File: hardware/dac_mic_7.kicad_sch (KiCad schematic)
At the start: 29 parts, among them J6 IMP34DT05, J7 SJ-3524-SMT, U6 CS43L22

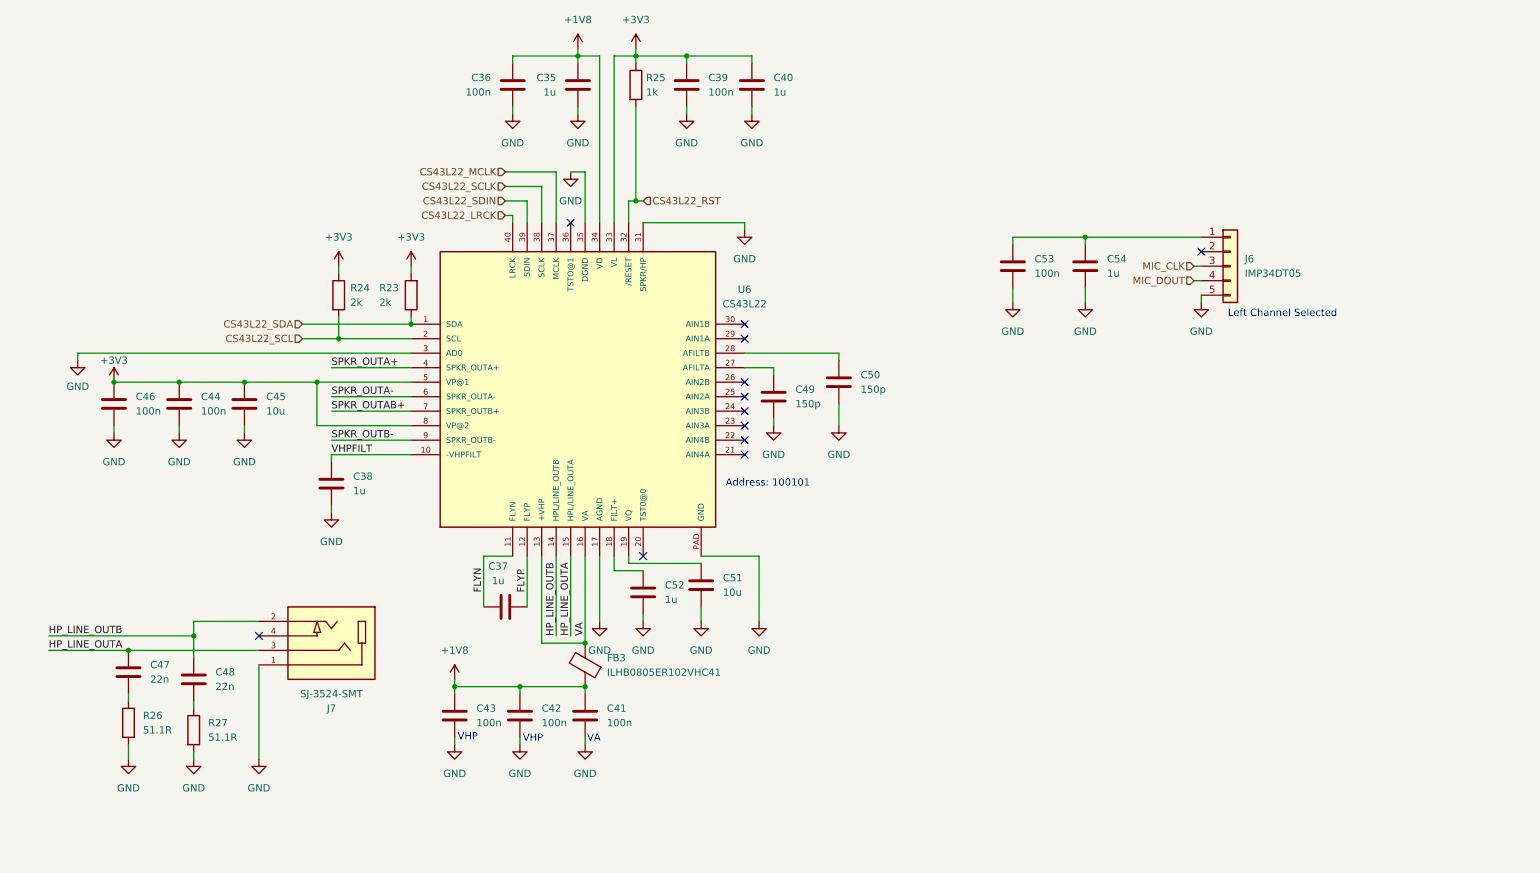
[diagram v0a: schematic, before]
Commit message: Design Schematic for STM32F407
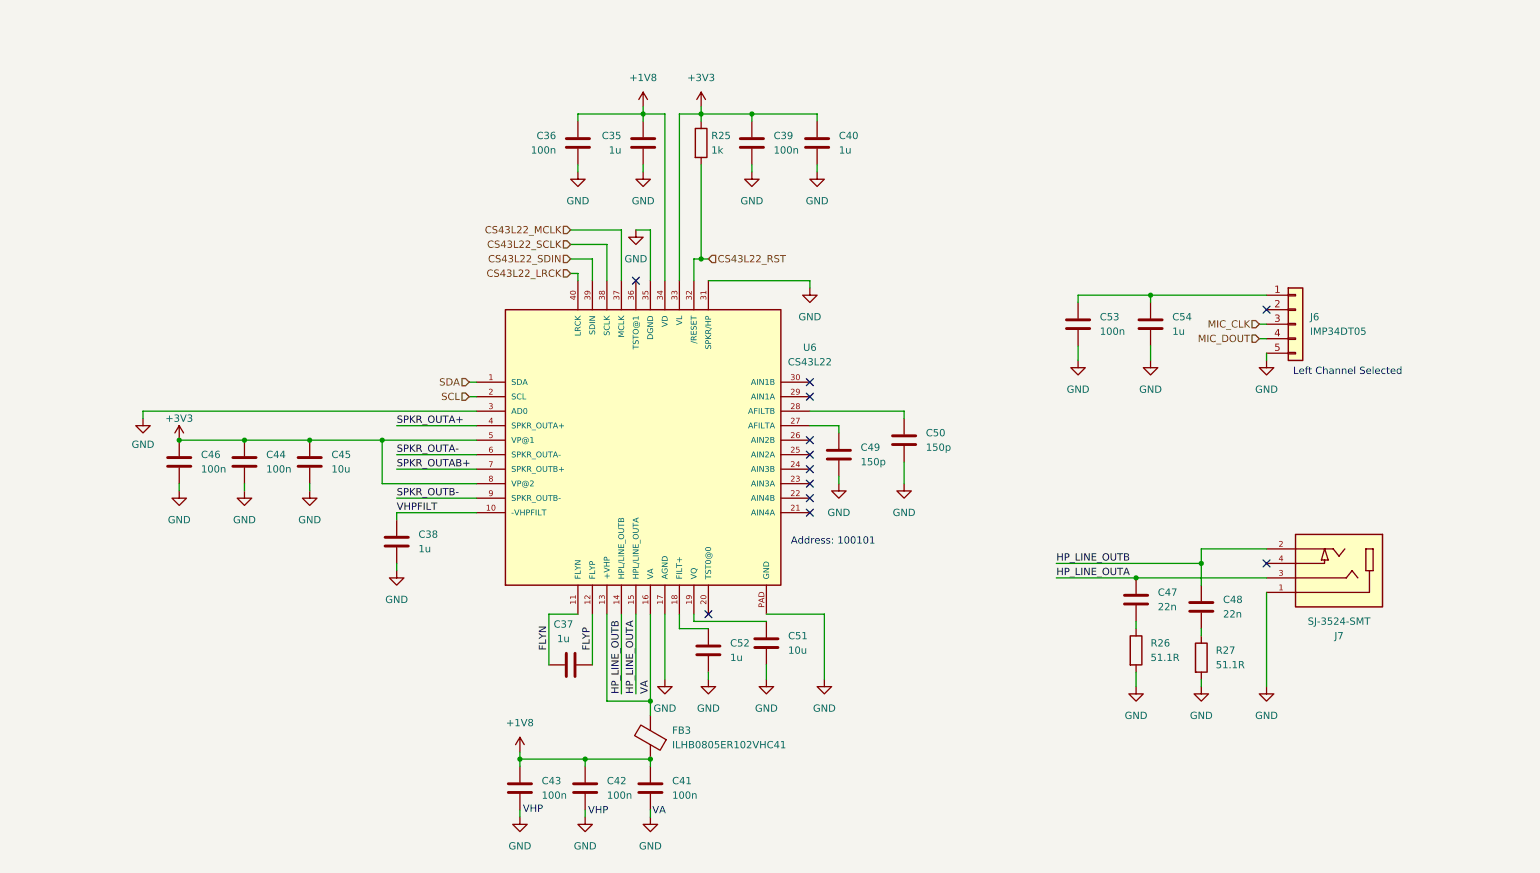
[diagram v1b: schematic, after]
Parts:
- removed R23, R24: 2k, symbol Device:R
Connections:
- net CS43L22_SCL renamed SCL
- net CS43L22_SDA renamed SDA
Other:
- moved on the sheet: C35, C36, C37, C38, C39, C40, C41, C42, C43, C44, C45, C46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

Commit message: Complete Schematic for Power Section
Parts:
- renumbered C46 to C34, C44 to C35, C45 to C36, C38 to C37, C43 to C38, C37 to C39, C36 to C40, C42 to C41, C35 to C42, C41 to C43, C52 to C44, C39 to C45, C51 to C46, C40 to C47, C49 to C48, C50 to C49, C53 to C50, C47 to C51, C54 to C52, C48 to C53, R25 to R20, R26 to R21, R27 to R22

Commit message: Organize schematic
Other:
- note added: "DAC"
- note added: "Headphones"
- note added: "Mic"
- moved on the sheet: C34, C35, C36, C37, C38, C39, C40, C41, C42, C43, C44, C45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

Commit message: Link footprints to Symbols
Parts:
- C34, C35, C40, C45, C49, C50: footprint (none) -> STM32F407 Dev Kit Library:C_0805_2012Metric_Pad1.18x1.45mm_HandSolder
- C36, C42, C47, C52: footprint SODFL1006X43N -> STM32F407 Dev Kit Library:C_0805_2012Metric_Pad1.18x1.45mm_HandSolder
- C37, C38, C39, C41, C43, C44, C46, C48, C51, C53: footprint Diode_SMD:ST_D_SMC -> STM32F407 Dev Kit Library:C_0805_2012Metric_Pad1.18x1.45mm_HandSolder
- FB3: footprint Package_DFN_QFN:QFN-16-1EP_4x4mm_P0.65mm_EP2.1x2.1mm -> STM32F407 Dev Kit Library:C_0805_2012Metric_Pad1.18x1.45mm_HandSolder
- J6: footprint Package_DFN_QFN:QFN-20-1EP_5x5mm_P0.65mm_EP3.35x3.35mm -> STM32F407 Dev Kit Library:IMP34DT06JTR
- J7: footprint SJ-3524-SMT:CUI_SJ-3524-SMT -> STM32F407 Dev Kit Library:SJ-3524-SMT
- R20, R21, R22: footprint (none) -> STM32F407 Dev Kit Library:R_0805_2012Metric_Pad1.20x1.40mm_HandSolder
- U6: footprint CS43L22:QFN40-6X6 -> STM32F407 Dev Kit Library:VQFN-40-1EP_6x6mm_P0.5mm_EP3.5x3.5mm
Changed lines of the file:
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@@
 			)
 		)
-		(property "Footprint" "Diode_SMD:ST_D_SMC"
+		(property "Footprint" "STM32F407 Dev Kit Library:C_0805_2012Metric_Pad1.18x1.45mm_HandSolder"
 			(at 212.3948 128.27 0)
 			(hide yes)
@@
 			)
 		)
-		(property "Footprint" ""
+		(property "Footprint" "STM32F407 Dev Kit Library:C_0805_2012Metric_Pad1.18x1.45mm_HandSolder"
 			(at 98.0948 41.91 0)
 			(hide yes)
@@
 			)
 		)
-		(property "Footprint" "SODFL1006X43N"
+		(property "Footprint" "STM32F407 Dev Kit Library:C_0805_2012Metric_Pad1.18x1.45mm_HandSolder"
 			(at 53.0352 97.79 0)
 			(hide yes)
@@
 			)
 		)
-		(property "Footprint" "Diode_SMD:ST_D_SMC"
+		(property "Footprint" "STM32F407 Dev Kit Library:C_0805_2012Metric_Pad1.18x1.45mm_HandSolder"
 			(at 145.7452 96.52 0)
 			(hide yes)
@@
 			)
 		)
-		(property "Footprint" "SJ-3524-SMT:CUI_SJ-3524-SMT"
+		(property "Footprint" "STM32F407 Dev Kit Library:SJ-3524-SMT"
 			(at 248.92 125.73 0)
 			(hide yes)
@@
 			)
 		)
-		(property "Footprint" "Package_DFN_QFN:QFN-16-1EP_4x4mm_P0.65mm_EP2.1x2.1mm"
+		(property "Footprint" "STM32F407 Dev Kit Library:C_0805_2012Metric_Pad1.18x1.45mm_HandSolder"
 			(at 113.538 142.24 90)
 			(hide yes)
@@
 			)
 		)
-		(property "Footprint" "Diode_SMD:ST_D_SMC"
+		(property "Footprint" "STM32F407 Dev Kit Library:C_0805_2012Metric_Pad1.18x1.45mm_HandSolder"
 			(at 66.3448 104.14 0)
 			(hide yes)
@@
 			)
 		)
-		(property "Footprint" "Diode_SMD:ST_D_SMC"
+		(property "Footprint" "STM32F407 Dev Kit Library:C_0805_2012Metric_Pad1.18x1.45mm_HandSolder"
 			(at 122.8852 130.81 0)
 			(hide yes)
@@
 			)
 		)
-		(property "Footprint" ""
+		(property "Footprint" "STM32F407 Dev Kit Library:C_0805_2012Metric_Pad1.18x1.45mm_HandSolder"
 			(at 30.1752 97.79 0)
 			(hide yes)
@@
 			)
 		)
-		(property "Footprint" ""
+		(property "Footprint" "STM32F407 Dev Kit Library:R_0805_2012Metric_Pad1.20x1.40mm_HandSolder"
 			(at 118.872 38.1 90)
 			(hide yes)
@@
 			)
 		)
-		(property "Footprint" "Package_DFN_QFN:QFN-20-1EP_5x5mm_P0.65mm_EP3.35x3.35mm"
+		(property "Footprint" "STM32F407 Dev Kit Library:IMP34DT06JTR"
 			(at 245.11 46.99 0)
 			(hide yes)
@@
 			)
 		)
-		(property "Footprint" "CS43L22:QFN40-6X6"
+		(property "Footprint" "STM32F407 Dev Kit Library:VQFN-40-1EP_6x6mm_P0.5mm_EP3.5x3.5mm"
 			(at 86.36 67.31 0)
 			(hide yes)
@@
 			)
 		)
-		(property "Footprint" ""
+		(property "Footprint" "STM32F407 Dev Kit Library:R_0805_2012Metric_Pad1.20x1.40mm_HandSolder"
 			(at 211.582 140.97 90)
 			(hide yes)
@@
 			)
 		)
-		(property "Footprint" "SODFL1006X43N"
+		(property "Footprint" "STM32F407 Dev Kit Library:C_0805_2012Metric_Pad1.18x1.45mm_HandSolder"
 			(at 141.9352 41.91 0)
 			(hide yes)
@@
 			)
 		)
-		(property "Footprint" "SODFL1006X43N"
+		(property "Footprint" "STM32F407 Dev Kit Library:C_0805_2012Metric_Pad1.18x1.45mm_HandSolder"
 			(at 220.6752 50.8 0)
 			(hide yes)
@@
 			)
 		)
-		(property "Footprint" "Diode_SMD:ST_D_SMC"
+		(property "Footprint" "STM32F407 Dev Kit Library:C_0805_2012Metric_Pad1.18x1.45mm_HandSolder"
 			(at 110.7948 147.32 0)
 			(hide yes)
@@
 			)
 		)
-		(property "Footprint" ""
+		(property "Footprint" "STM32F407 Dev Kit Library:C_0805_2012Metric_Pad1.18x1.45mm_HandSolder"
 			(at 207.9752 50.8 0)
 			(hide yes)
@@
 			)
 		)
-		(property "Footprint" ""
+		(property "Footprint" "STM32F407 Dev Kit Library:R_0805_2012Metric_Pad1.20x1.40mm_HandSolder"
 			(at 223.012 142.24 90)
 			(hide yes)
@@
 			)
 		)
-		(property "Footprint" "Diode_SMD:ST_D_SMC"
+		(property "Footprint" "STM32F407 Dev Kit Library:C_0805_2012Metric_Pad1.18x1.45mm_HandSolder"
 			(at 133.0452 129.54 0)
 			(hide yes)
@@
 			)
 		)
-		(property "Footprint" "SODFL1006X43N"
+		(property "Footprint" "STM32F407 Dev Kit Library:C_0805_2012Metric_Pad1.18x1.45mm_HandSolder"
 			(at 109.5248 41.91 0)
 			(hide yes)
@@
 			)
 		)
-		(property "Footprint" ""
+		(property "Footprint" "STM32F407 Dev Kit Library:C_0805_2012Metric_Pad1.18x1.45mm_HandSolder"
 			(at 130.5052 41.91 0)
 			(hide yes)
@@
 			)
 		)
-		(property "Footprint" "Diode_SMD:ST_D_SMC"
+		(property "Footprint" "STM32F407 Dev Kit Library:C_0805_2012Metric_Pad1.18x1.45mm_HandSolder"
 			(at 87.9348 147.32 0)
 			(hide yes)
@@
 			)
 		)
-		(property "Footprint" "Diode_SMD:ST_D_SMC"
+		(property "Footprint" "STM32F407 Dev Kit Library:C_0805_2012Metric_Pad1.18x1.45mm_HandSolder"
 			(at 223.8248 129.54 0)
 			(hide yes)
@@
 			)
 		)
-		(property "Footprint" ""
+		(property "Footprint" "STM32F407 Dev Kit Library:C_0805_2012Metric_Pad1.18x1.45mm_HandSolder"
 			(at 157.1752 93.98 0)
 			(hide yes)
@@
 			)
 		)
-		(property "Footprint" "Diode_SMD:ST_D_SMC"
+		(property "Footprint" "STM32F407 Dev Kit Library:C_0805_2012Metric_Pad1.18x1.45mm_HandSolder"
 			(at 99.3648 147.32 0)
 			(hide yes)
@@
 			)
 		)
-		(property "Footprint" "Diode_SMD:ST_D_SMC"
+		(property "Footprint" "STM32F407 Dev Kit Library:C_0805_2012Metric_Pad1.18x1.45mm_HandSolder"
 			(at 101.6 128.5748 0)
 			(hide yes)
@@
 			)
 		)
-		(property "Footprint" ""
+		(property "Footprint" "STM32F407 Dev Kit Library:C_0805_2012Metric_Pad1.18x1.45mm_HandSolder"
 			(at 41.6052 97.79 0)
 			(hide yes)

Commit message: Convert Schematic to PCB
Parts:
- removed J6: IMP34DT05, STM32F407 Dev Kit Library:IMP34DT06JTR, symbol STM32F407 Dev Kit Library:Conn_01x05
- added J12: IMP34DT05, STM32F407 Dev Kit Library:IMP34DT06JTR, symbol Connector_Generic:Conn_01x08
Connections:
- net GND: now also J12.5 (Pin_5), J12.6 (Pin_6), J12.7 (Pin_7), J12.8 (Pin_8)
- net MIC_CLK: now also J12.3 (Pin_3)
- net MIC_DOUT: now also J12.4 (Pin_4)
- net at C50.1, C52.1: now also J12.1 (Pin_1)

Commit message: Place components for DAC and Mic
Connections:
- net +3V3: now also C50.1, C52.1, J12.1 (Pin_1)
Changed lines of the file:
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@@
+	)
+	(junction
+		(at 207.01 41.91)
+		(diameter 0)
+		(color 0 0 0 0)
 	)
 	(junction
@@
 		(pts
 			(xy 40.64 99.06) (xy 40.64 97.79)
+		)
+		(stroke
+			(width 0)
+			(type default)
+		)
+	)
+	(wire
+		(pts
+			(xy 207.01 40.64) (xy 207.01 41.91)
 		)
 		(stroke
@@
 					(unit 1)
 				)
+			)
+		)
+	)
+	(symbol
+		(lib_id "power:+3V3")
+		(at 207.01 40.64 0)
+		(unit 1)
+		(body_style 1)
+		(exclude_from_sim no)
+		(in_bom yes)
+		(on_board yes)
+		(in_pos_files yes)
+		(dnp no)
+		(fields_autoplaced yes)
+		(property "Reference" "#PWR0138"
+			(at 207.01 44.45 0)
+			(hide yes)
+			(show_name no)
+			(do_not_autoplace no)
+			(effects
+				(font
+					(size 1.27 1.27)
+				)
+			)
+		)
+		(property "Value" "+3V3"
+			(at 207.01 35.56 0)
+			(show_name no)
+			(do_not_autoplace no)
+			(effects
+				(font
+					(size 1.27 1.27)
+				)
+			)
+		)
+		(property "Footprint" ""
+			(at 207.01 40.64 0)
+			(hide yes)
+			(show_name no)
+			(do_not_autoplace no)
+			(effects
+				(font
+					(size 1.27 1.27)
+				)
+			)
+		)
+		(property "Datasheet" ""
+			(at 207.01 40.64 0)
+			(hide yes)
+			(show_name no)
+			(do_not_autoplace no)
+			(effects
+				(font
+					(size 1.27 1.27)
+				)
+			)
+		)
+		(property "Description" "Power symbol creates a global label with name \"+3V3\""
+			(at 207.01 40.64 0)
+			(hide yes)
+			(show_name no)
+			(do_not_autoplace no)
+			(effects
+				(font
+					(size 1.27 1.27)
+				)
+			)
+		)
+		(pin "1"
+		)
+		(instances
+			(project "STM32F407 Dev Kit"
+				(path "/f3d27387-fbda-4c9d-aea0-93d92d34cd17/6f0c22b1-7361-42cd-874f-7f49f54e5538"
+					(reference "#PWR0138")
+					(unit 1)
+				)

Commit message: Route Ethernet section and add global labels
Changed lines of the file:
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@@
 		)
 	)
-	(hierarchical_label "CS43L22_RST"
+	(global_label "MIC_DOUT"
+		(shape input)
+		(at 238.76 49.53 180)
+		(fields_autoplaced yes)
+		(effects
+			(font
+				(size 1.27 1.27)
+			)
+			(justify right)
+		)
+		(property "Intersheetrefs" "${INTERSHEET_REFS}"
+			(at 226.5824 49.53 0)
+			(hide yes)
+			(show_name no)
+			(do_not_autoplace no)
+			(effects
+				(font
+					(size 1.27 1.27)
+				)
+				(justify right)
+			)
+		)
+	)
+	(global_label "CS43L22_SDIN"
+		(shape input)
+		(at 97.79 58.42 180)
+		(fields_autoplaced yes)
+		(effects
+			(font
+				(size 1.27 1.27)
+			)
+			(justify right)
+		)
+		(property "Intersheetrefs" "${INTERSHEET_REFS}"
+			(at 81.0768 58.42 0)
+			(hide yes)
+			(show_name no)
+			(do_not_autoplace no)
+			(effects
+				(font
+					(size 1.27 1.27)
+				)
+				(justify right)
+			)
+		)
+	)
+	(global_label "CS43L22_LRCK"
+		(shape input)
+		(at 97.79 60.96 180)
+		(fields_autoplaced yes)
+		(effects
+			(font
+				(size 1.27 1.27)
+			)
+			(justify right)
+		)
+		(property "Intersheetrefs" "${INTERSHEET_REFS}"
+			(at 80.6535 60.96 0)
+			(hide yes)
+			(show_name no)
+			(do_not_autoplace no)
+			(effects
+				(font
+					(size 1.27 1.27)
+				)
+				(justify right)
+			)
+		)
+	)
+	(global_label "SCL"
+		(shape input)
+		(at 80.01 82.55 180)
+		(fields_autoplaced yes)
+		(effects
+			(font
+				(size 1.27 1.27)
+			)
+			(justify right)
+		)
+		(property "Intersheetrefs" "${INTERSHEET_REFS}"
+			(at 73.5172 82.55 0)
+			(hide yes)
+			(show_name no)
+			(do_not_autoplace no)
+			(effects
+				(font
+					(size 1.27 1.27)
+				)
+				(justify right)
+			)
+		)
+	)
+	(global_label "MIC_CLK"
+		(shape input)
+		(at 238.76 46.99 180)
+		(fields_autoplaced yes)
+		(effects
+			(font
+				(size 1.27 1.27)
+			)
+			(justify right)
+		)
+		(property "Intersheetrefs" "${INTERSHEET_REFS}"
+			(at 227.9129 46.99 0)
+			(hide yes)
+			(show_name no)
+			(do_not_autoplace no)
+			(effects
+				(font
+					(size 1.27 1.27)
+				)
+				(justify right)
+			)
+		)
+	)
+	(global_label "SDA"
+		(shape input)
+		(at 80.01 80.01 180)
+		(fields_autoplaced yes)
+		(effects
+			(font
+				(size 1.27 1.27)
+			)
+			(justify right)
+		)
+		(property "Intersheetrefs" "${INTERSHEET_REFS}"
+			(at 73.4567 80.01 0)
+			(hide yes)
+			(show_name no)
+			(do_not_autoplace no)
+			(effects
+				(font
+					(size 1.27 1.27)
+				)
+				(justify right)
+			)
+		)
+	)
+	(global_label "CS43L22_SCLK"
+		(shape input)
+		(at 97.79 55.88 180)
+		(fields_autoplaced yes)
+		(effects
+			(font
+				(size 1.27 1.27)
+			)
+			(justify right)
+		)
+		(property "Intersheetrefs" "${INTERSHEET_REFS}"
+			(at 80.714 55.88 0)
+			(hide yes)
+			(show_name no)
+			(do_not_autoplace no)
+			(effects
+				(font
+					(size 1.27 1.27)
+				)
+				(justify right)
+			)
+		)
+	)
+	(global_label "CS43L22_RST"
 		(shape input)
 		(at 121.92 58.42 0)
+		(fields_autoplaced yes)
 		(effects
 			(font
@@
 			(justify left)
 		)
-	)
-	(hierarchical_label "CS43L22_SCLK"
-		(shape input)
-		(at 97.79 55.88 180)
-		(effects
-			(font
-				(size 1.27 1.27)
-			)
-			(justify right)
-		)
-	)
-	(hierarchical_label "CS43L22_SDIN"
-		(shape input)
-		(at 97.79 58.42 180)
-		(effects
-			(font
-				(size 1.27 1.27)
-			)
-			(justify right)
-		)
-	)
-	(hierarchical_label "SDA"
-		(shape input)
-		(at 80.01 80.01 180)
-		(effects
-			(font
-				(size 1.27 1.27)
-			)
-			(justify right)
-		)
-	)
-	(hierarchical_label "CS43L22_LRCK"
-		(shape input)
-		(at 97.79 60.96 180)
-		(effects
-			(font
-				(size 1.27 1.27)
-			)
-			(justify right)
-		)
-	)
-	(hierarchical_label "SCL"
-		(shape input)
-		(at 80.01 82.55 180)
-		(effects
-			(font
-				(size 1.27 1.27)
-			)
-			(justify right)
-		)
-	)
-	(hierarchical_label "MIC_CLK"
-		(shape input)
-		(at 238.76 46.99 180)
-		(effects
-			(font
-				(size 1.27 1.27)
-			)
-			(justify right)
-		)
-	)
-	(hierarchical_label "CS43L22_MCLK"
+		(property "Intersheetrefs" "${INTERSHEET_REFS}"
+			(at 137.6655 58.42 0)
+			(hide yes)
+			(show_name no)
+			(do_not_autoplace no)
+			(effects
+				(font
+					(size 1.27 1.27)
+				)
+				(justify left)
+			)
+		)
+	)
+	(global_label "CS43L22_MCLK"
 		(shape input)
 		(at 97.79 53.34 180)
-		(effects
-			(font
-				(size 1.27 1.27)
-			)
-			(justify right)
-		)
-	)
-	(hierarchical_label "MIC_DOUT"
-		(shape input)
-		(at 238.76 49.53 180)
-		(effects
-			(font
-				(size 1.27 1.27)
-			)
-			(justify right)
-		)
-	)
+		(fields_autoplaced yes)
+		(effects
+			(font
+				(size 1.27 1.27)
+			)
+			(justify right)
+		)
+		(property "Intersheetrefs" "${INTERSHEET_REFS}"
+			(at 80.4721 53.34 0)
+			(hide yes)
+			(show_name no)
+			(do_not_autoplace no)
+			(effects
+				(font
+					(size 1.27 1.27)
+				)
+				(justify right)
+			)
+		)
+	)
